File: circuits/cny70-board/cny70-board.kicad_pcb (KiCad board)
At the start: 2 copper layers, 129 x 22.5 mm, 25 parts, among them J1 Out, Q1 2N3904, Q2 2N3904, Q3 2N3904, Q4 2N3904, U1 CNY70, U2 CNY70, U3 CNY70, U4 CNY70

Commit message: New CNY70 board
Changes in tracks and spacings to match new configuration on CNC.
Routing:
- net GND: track 185.5 -> 0.00 mm
- net +5V: track 233.1 -> 202.6 mm, vias 4 -> 8
- net /S4: track 58.1 -> 43.4 mm
- net Net-(U2-A): track 21.0 -> 16.8 mm
- net Net-(U4-A): track 21.0 -> 16.9 mm
- net /S1: track 128.8 -> 125.0 mm
- net /S3: track 76.9 -> 80.1 mm
- net Net-(U1-A): track 23.3 -> 25.6 mm
- net /S2: track 111.5 -> 110.3 mm
- net Net-(Q4-B): track 8.06 -> 8.81 mm

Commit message: Grb and Drl for CNY70 board - V0.1
Grb and Drl for CNY70 board - V0.1
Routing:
- net +5V: track 202.6 -> 196.4 mm
- net Net-(U3-A): track 23.0 -> 25.0 mm
- net Net-(Q4-B): track 8.81 -> 9.64 mm
- net /S2: track 110.3 -> 111.1 mm
- net Net-(U1-A): track 25.6 -> 26.2 mm

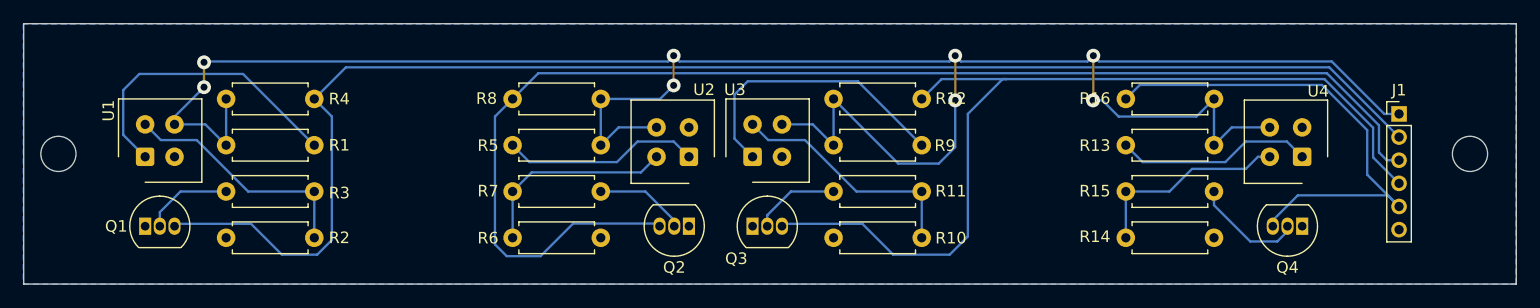
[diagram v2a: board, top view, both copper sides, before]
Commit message: Line width changed
Path/spaces are now 0.3048/0.3048 mm (12/12 mil), and vias are 1.6-0.8 mm
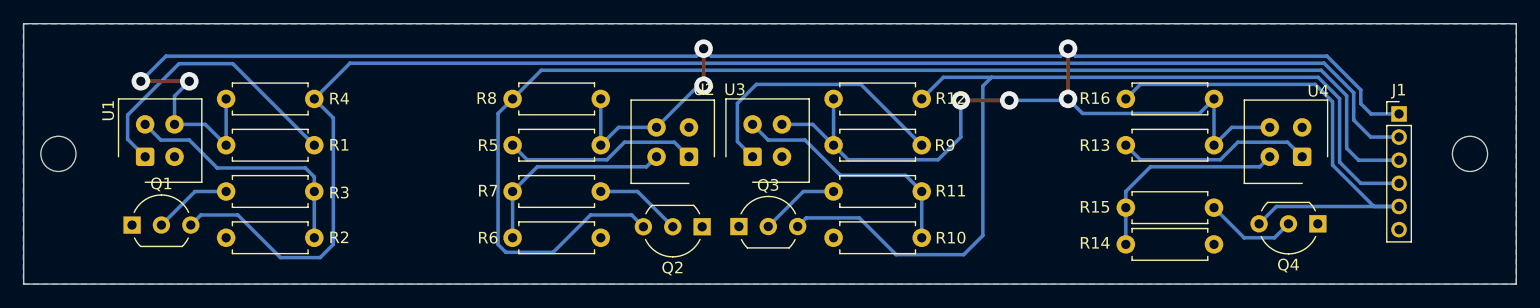
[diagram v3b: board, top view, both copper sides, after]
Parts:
- Q1, Q2, Q3, Q4: footprint Package_TO_SOT_THT:TO-92_Inline -> Package_TO_SOT_THT:TO-92_Inline_Wide
- moved R15 1.40 mm to (180.3, 100.7)
- moved Q4 1.37 mm to (196.8, 102.1)
- moved Q3 1.18 mm to (146.8, 102.3)
- moved Q2 1.14 mm to (143.6, 102.4)
- moved Q1 1.14 mm to (94.4, 102.2)
- moved R14 0.57 mm to (180.3, 103.9)
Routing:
- net +5V: track 196.4 -> 210.8 mm
- net Net-(Q4-B): track 9.64 -> 8.01 mm
- net /S1: track 125.5 -> 127.0 mm
- net Net-(U1-A): track 26.2 -> 25.1 mm
- net /S3: track 80.3 -> 81.3 mm
- net Net-(U3-A): track 25.0 -> 23.9 mm
- net /S4: track 43.4 -> 44.4 mm
- net Net-(Q1-B): track 7.68 -> 6.79 mm
- net Net-(U1-E): track 21.0 -> 21.8 mm
- net Net-(Q3-B): track 7.53 -> 6.90 mm
- net Net-(U4-E): track 17.7 -> 18.3 mm
